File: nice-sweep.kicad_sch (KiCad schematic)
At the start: 72 parts, among them SW1 Kailh-Choc, SW10 Kailh-Choc, SW11 Kailh-Choc, SW12 Kailh-Choc, SW13 Kailh-Choc, SW14 Kailh-Choc, SW15 Kailh-Choc, SW16 Kailh-Choc, SW17 Kailh-Choc, SW18 Kailh-Choc, SW19 Kailh-Choc, SW2 Kailh-Choc, SW20 Kailh-Choc, SW21 Kailh-Choc, SW22 Kailh-Choc, SW23 Kailh-Choc, SW24 Kailh-Choc, SW25 Kailh-Choc, SW26 Kailh-Choc, SW27 Kailh-Choc, SW28 Kailh-Choc, SW29 Kailh-Choc, SW3 Kailh-Choc, SW30 Kailh-Choc, SW31 Kailh-Choc, SW32 Kailh-Choc, SW33 Kailh-Choc, SW34 Kailh-Choc, SW4 Kailh-Choc, SW5 Kailh-Choc, SW6 Kailh-Choc, SW7 Kailh-Choc, SW8 Kailh-Choc, SW9 Kailh-Choc, U1 nice_nano, U2 nice_nano

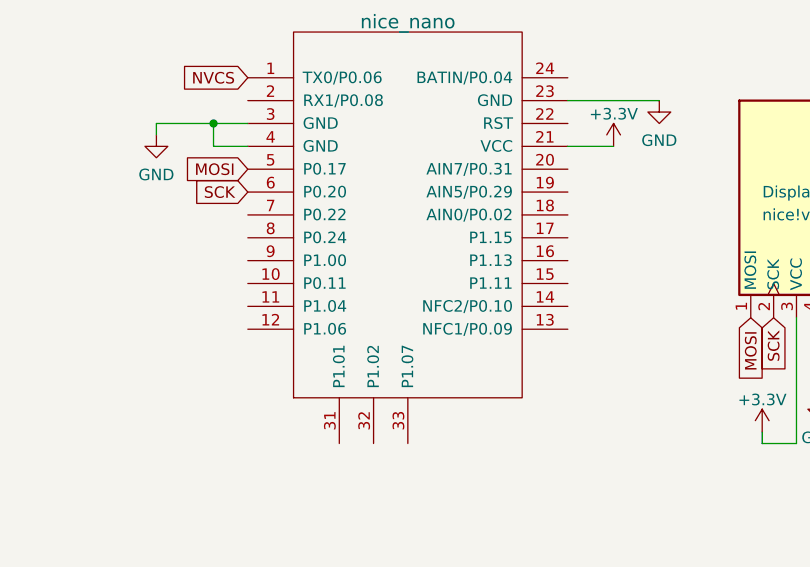
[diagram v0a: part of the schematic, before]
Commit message: Fix nice!nano orientation & add labels
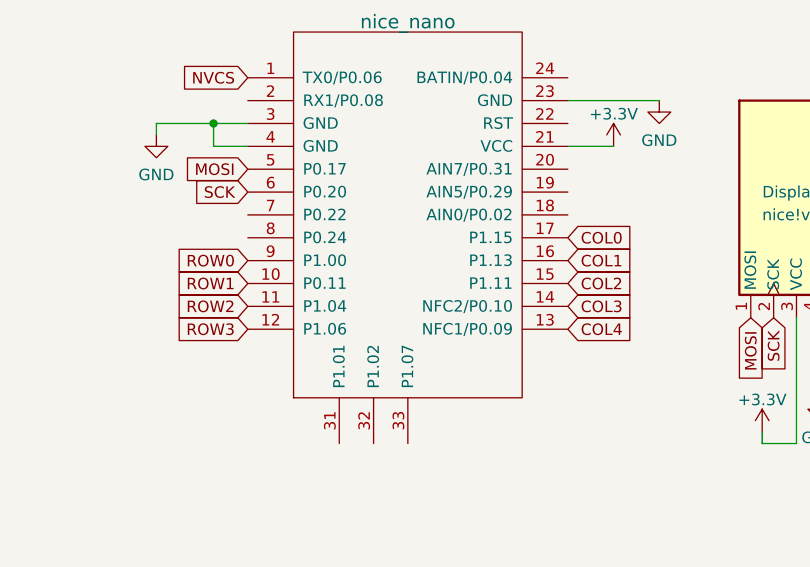
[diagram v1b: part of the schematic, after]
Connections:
- net COL0: now also U1.17 (P1.15)
- net COL1: now also U1.16 (P1.13)
- net COL2: now also U1.15 (P1.11)
- net COL3: now also U1.14 (NFC2/P0.10)
- net COL4: now also U1.13 (NFC1/P0.09)
- net ROW0: now also U1.9 (P1.00)
- net ROW1: now also U1.10 (P0.11)
- net ROW2: now also U1.11 (P1.04)
- net ROW3: now also U1.12 (P1.06)
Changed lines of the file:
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@@
+    )
+  )
+  (global_label "COL3" (shape input) (at 143.51 54.61 0) (fields_autoplaced)
+    (effects (font (size 1.27 1.27)) (justify left))
+    (property "Intersheet References" "${INTERSHEET_REFS}" (id 0) (at 150.7612 54.5306 0)
+      (effects (font (size 1.27 1.27)) (justify left) hide)
     )
   )
@@
     (property "Intersheet References" "${INTERSHEET_REFS}" (id 0) (at 135.8106 111.1612 90)
       (effects (font (size 1.27 1.27)) (justify left) hide)
+    )
+  )
+  (global_label "COL1" (shape input) (at 143.51 49.53 0) (fields_autoplaced)
+    (effects (font (size 1.27 1.27)) (justify left))
+    (property "Intersheet References" "${INTERSHEET_REFS}" (id 0) (at 150.7612 49.4506 0)
+      (effects (font (size 1.27 1.27)) (justify left) hide)
+    )
+  )
+  (global_label "ROW1" (shape input) (at 107.95 52.07 180) (fields_autoplaced)
+    (effects (font (size 1.27 1.27)) (justify right))
+    (property "Intersheet References" "${INTERSHEET_REFS}" (id 0) (at 100.2755 51.9906 0)
+      (effects (font (size 1.27 1.27)) (justify right) hide)
+    )
+  )
+  (global_label "ROW0" (shape input) (at 107.95 49.53 180) (fields_autoplaced)
+    (effects (font (size 1.27 1.27)) (justify right))
+    (property "Intersheet References" "${INTERSHEET_REFS}" (id 0) (at 100.2755 49.4506 0)
+      (effects (font (size 1.27 1.27)) (justify right) hide)
     )
   )
@@
     )
   )
+  (global_label "ROW3" (shape input) (at 107.95 57.15 180) (fields_autoplaced)
+    (effects (font (size 1.27 1.27)) (justify right))
+    (property "Intersheet References" "${INTERSHEET_REFS}" (id 0) (at 100.2755 57.0706 0)
+      (effects (font (size 1.27 1.27)) (justify right) hide)
+    )
+  )
   (global_label "COL2" (shape input) (at 57.15 24.13 90) (fields_autoplaced)
     (effects (font (size 1.27 1.27)) (justify left))
     (property "Intersheet References" "${INTERSHEET_REFS}" (id 0) (at 57.0706 16.8788 90)
+      (effects (font (size 1.27 1.27)) (justify left) hide)
+    )
+  )
+  (global_label "COL2" (shape input) (at 143.51 52.07 0) (fields_autoplaced)
+    (effects (font (size 1.27 1.27)) (justify left))
+    (property "Intersheet References" "${INTERSHEET_REFS}" (id 0) (at 150.7612 51.9906 0)
       (effects (font (size 1.27 1.27)) (justify left) hide)
     )
@@
     )
   )
+  (global_label "COL4" (shape input) (at 143.51 57.15 0) (fields_autoplaced)
+    (effects (font (size 1.27 1.27)) (justify left))
+    (property "Intersheet References" "${INTERSHEET_REFS}" (id 0) (at 150.7612 57.0706 0)
+      (effects (font (size 1.27 1.27)) (justify left) hide)
+    )
+  )
   (global_label "R_ROW1" (shape input) (at 157.48 154.94 0) (fields_autoplaced)
     (effects (font (size 1.27 1.27)) (justify left))
@@
     (effects (font (size 1.27 1.27)) (justify right))
     (property "Intersheet References" "${INTERSHEET_REFS}" (id 0) (at 100.9407 39.4494 0)
+      (effects (font (size 1.27 1.27)) (justify right) hide)
+    )
+  )
+  (global_label "ROW2" (shape input) (at 107.95 54.61 180) (fields_autoplaced)
+    (effects (font (size 1.27 1.27)) (justify right))
+    (property "Intersheet References" "${INTERSHEET_REFS}" (id 0) (at 100.2755 54.5306 0)
       (effects (font (size 1.27 1.27)) (justify right) hide)
     )
@@
       (effects (font (size 1.27 1.27)) (justify left) hide)
     )
+  )
+  (global_label "COL0" (shape input) (at 143.51 46.99 0) (fields_autoplaced)
+    (effects (font (size 1.27 1.27)) (justify left))
+    (property "Intersheet References" "${INTERSHEET_REFS}" (id 0) (at 150.7612 46.9106 0)
+      (effects (font (size 1.27 1.27)) (justify left) hide)
+    )

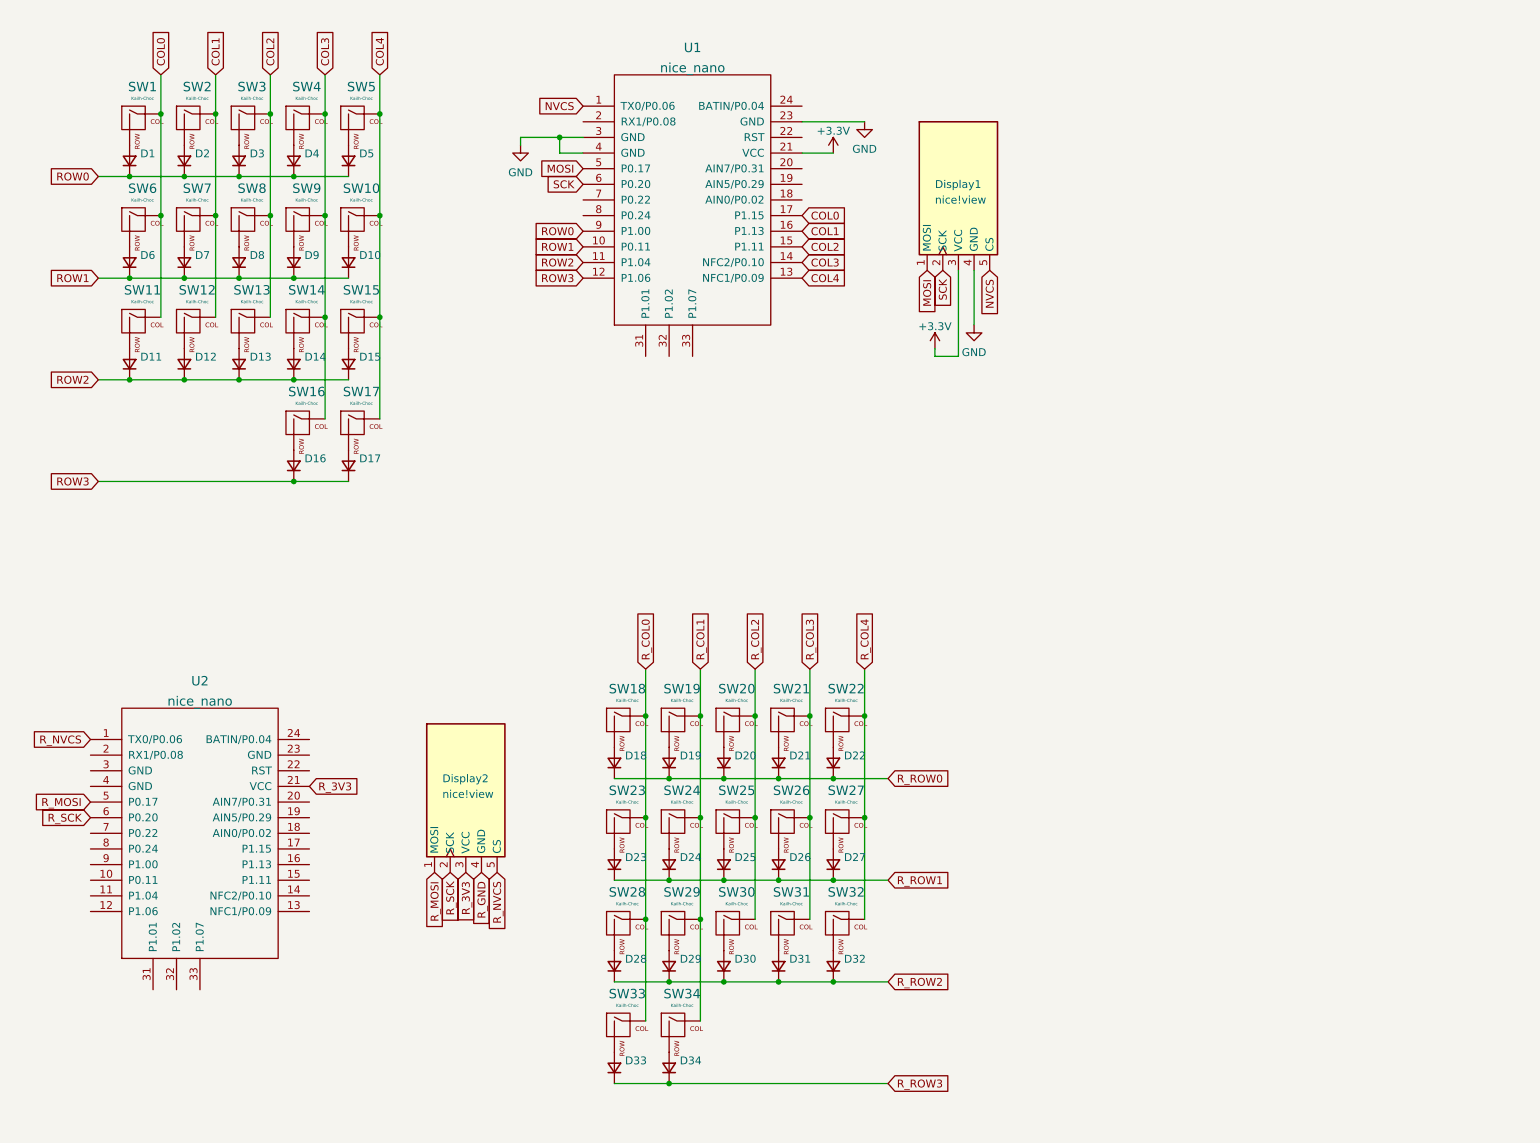
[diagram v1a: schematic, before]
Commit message: Update PCB with missing components
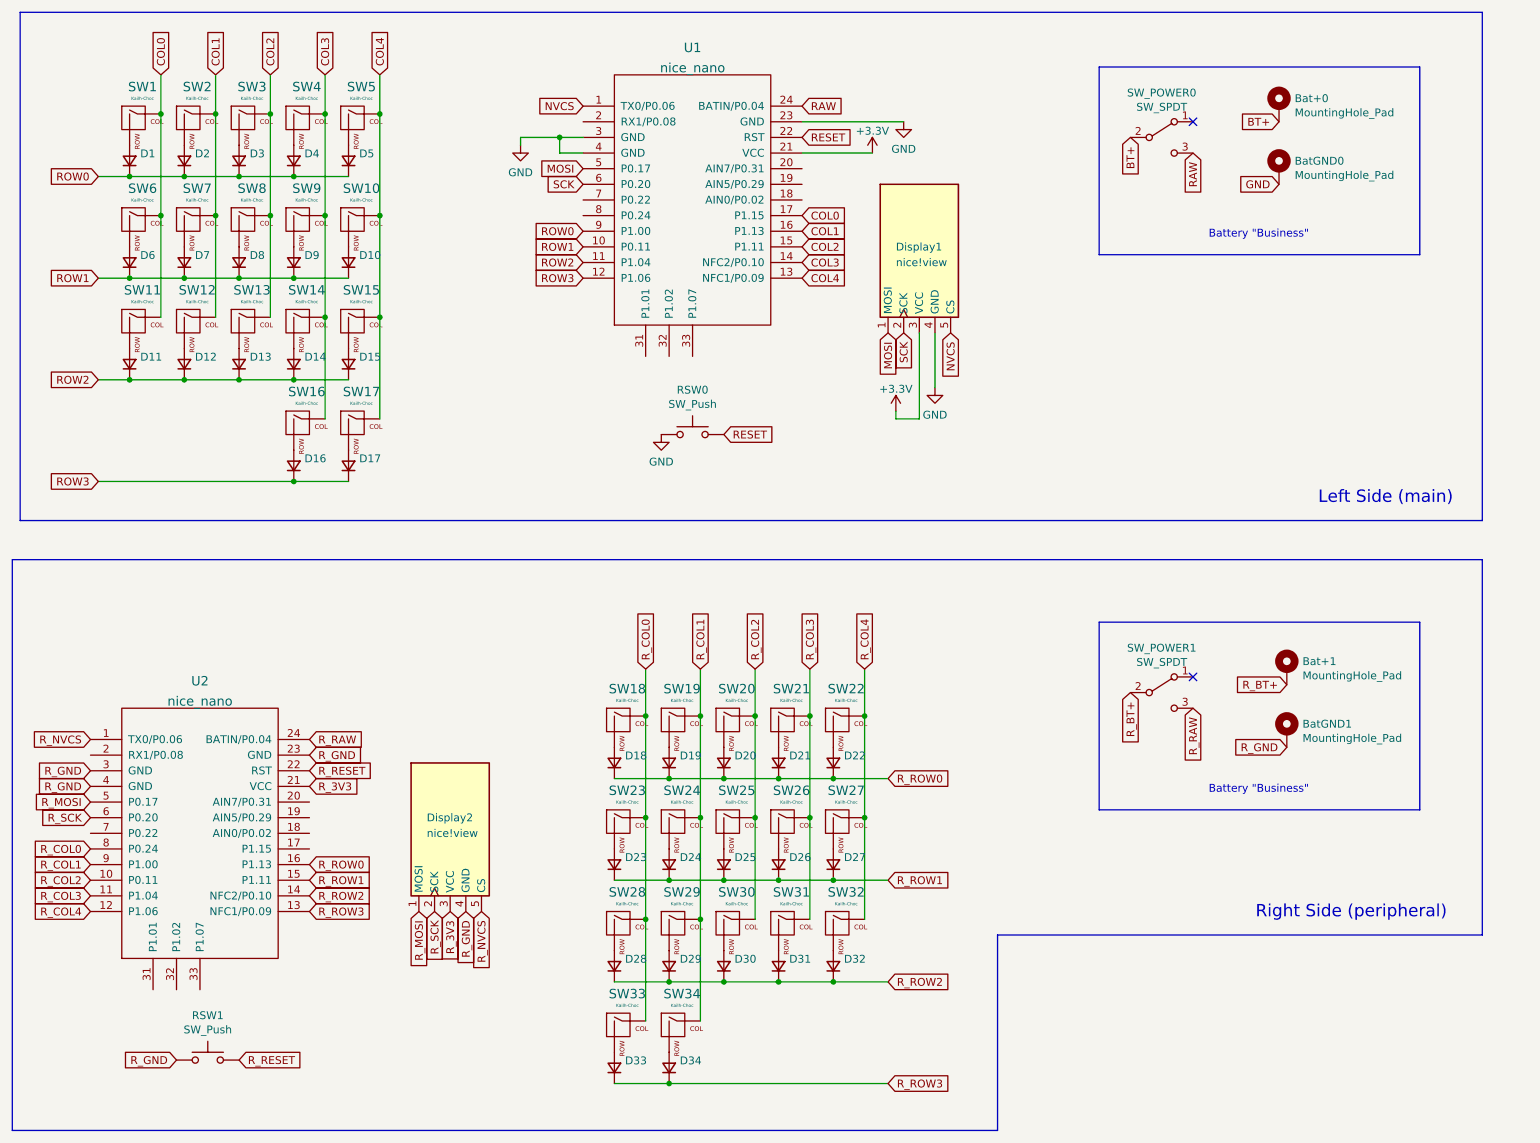
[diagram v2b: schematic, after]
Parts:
- added Bat+0, Bat+1, BatGND0, BatGND1: MountingHole_Pad, * duckyb-collection:1pin_conn, symbol Mechanical:MountingHole_Pad
- added RSW0, RSW1: SW_Push, * duckyb-collection:SW_RESET, symbol Switch:SW_Push
- added SW_POWER0, SW_POWER1: SW_SPDT, * duckyb-collection:SPDT_C128955, symbol Switch:SW_SPDT
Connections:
- net GND: now also BatGND0.1, RSW0.1
- net R_COL0: now also U2.8 (P0.24)
- net R_COL1: now also U2.9 (P1.00)
- net R_COL2: now also U2.10 (P0.11)
- net R_COL3: now also U2.11 (P1.04)
- net R_COL4: now also U2.12 (P1.06)
- net R_GND: now also U2.23 (GND), U2.3 (GND), U2.4 (GND), BatGND1.1, RSW1.1
- net R_ROW0: now also U2.16 (P1.13)
- net R_ROW1: now also U2.15 (P1.11)
- net R_ROW2: now also U2.14 (NFC2/P0.10)
- net R_ROW3: now also U2.13 (NFC1/P0.09)
- net RESET: now reaches U1.22 (RST)
- net RESET: now also RSW0.2
- net RAW: now reaches U1.24 (BATIN/P0.04)
- net RAW: now also SW_POWER0.3 (C)
- net R_RESET: now reaches U2.22 (RST)
- net R_RESET: now also RSW1.2
- net R_RAW: now reaches U2.24 (BATIN/P0.04)
- net R_RAW: now also SW_POWER1.3 (C)
- new net BT+: Bat+0.1, SW_POWER0.2 (B)
- new net R_BT+: Bat+1.1, SW_POWER1.2 (B)
- no-connect marks 0 -> 2
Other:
- note added: "Battery "Business""
- note added: "Left Side (main)"
- note added: "Right Side (peripheral)"
- moved on the sheet: Display1, Display2
